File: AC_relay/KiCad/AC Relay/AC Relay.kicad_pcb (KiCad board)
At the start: 2 copper layers, 49.5 x 49.5 mm, 17 parts, among them J1 Screw_Terminal_01x02, J2 Conn_01x06_Female, J3 Screw_Terminal_01x02, K1 1461492-2, Q1 FDN537N, SW1 SW_Push, U1 BU33SD5WG-TR, U2 ESP-12E, U3 HLK-PM01

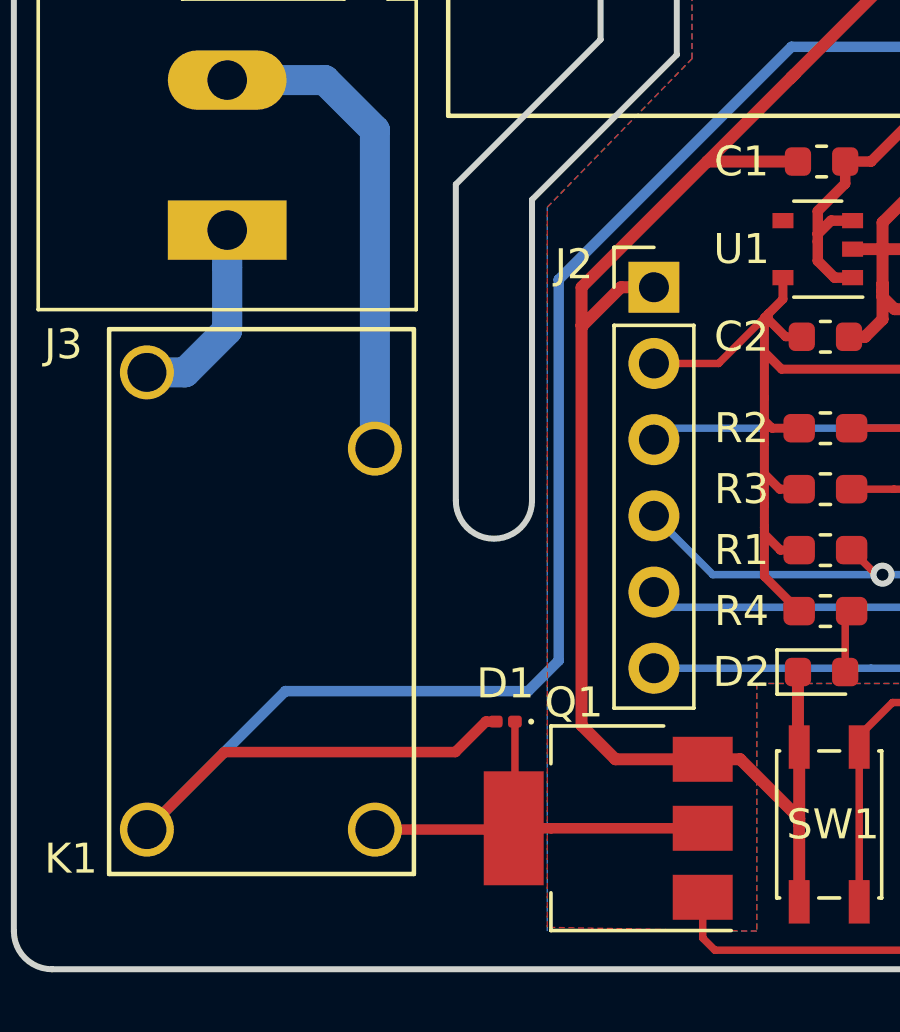
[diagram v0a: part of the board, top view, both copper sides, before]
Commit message: Diode footprint fised
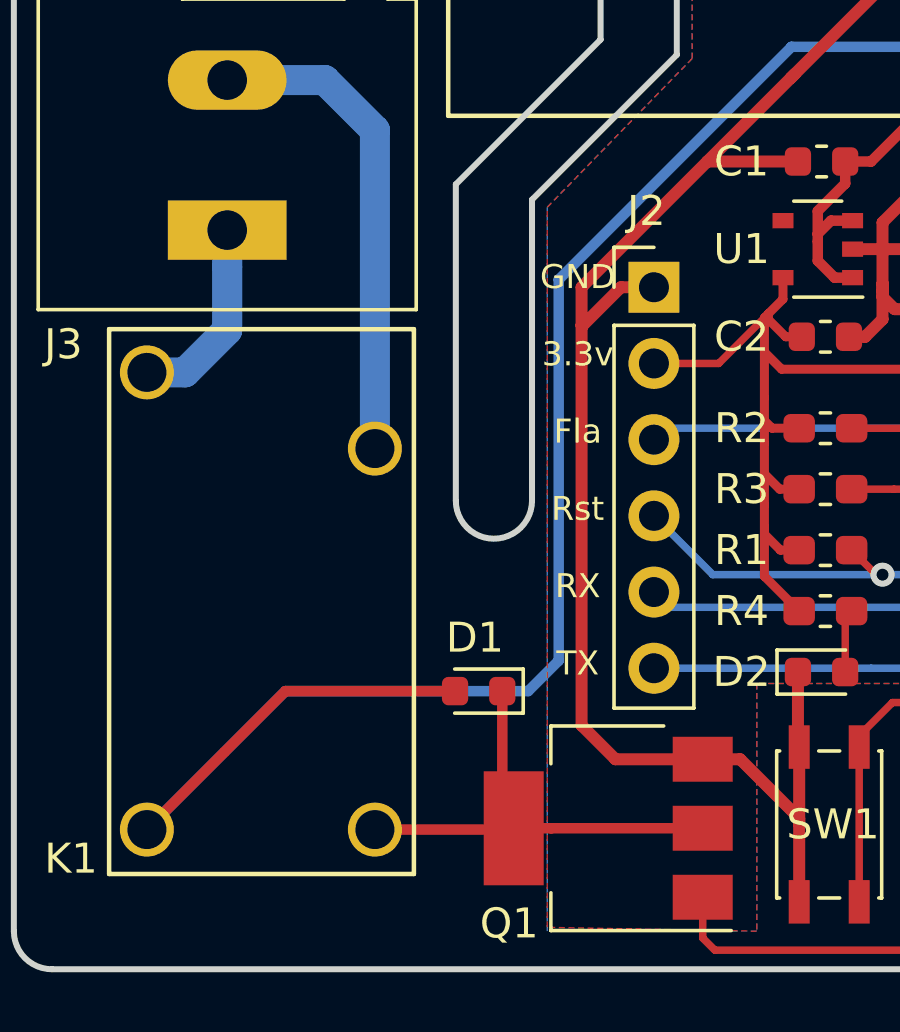
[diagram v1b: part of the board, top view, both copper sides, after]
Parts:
- D1: footprint Diode_SMD:D_0201_0603Metric -> Diode_SMD:D_0603_1608Metric
- moved D1 1.35 mm to (84.1, 87.2)
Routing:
- net Net-(D1-Pad1): track 14.5 -> 15.7 mm
- net +5V: track 99.6 -> 98.6 mm
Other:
- board text added: "AC Relay - ESP8266 Design by Enrique Gómez CC BY-SA 4.0 www.rinconingenieril.es Rev.: 2.1 - S/N:"
- board text added: "GND 3.3v Fla Rst RX TX"
- board text removed: "AC Relay - ESP8266 Design by Enrique Gómez CC BY-SA 4.0 www.rinconingenieril.es Rev.: 2.0 - S/N:"
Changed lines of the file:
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@@
   (general
     (thickness 1.6)
-    (drawings 28)
+    (drawings 29)
     (tracks 158)
     (zones 0)
@@
       (padsonsilk false)
       (subtractmaskfromsilk false)
-      (outputformat 4)
+      (outputformat 1)
       (mirror false)
       (drillshape 0)
       (scaleselection 1)
-      (outputdirectory "../../Manufacturing_GERBERs/AC_Relay/"))
+      (outputdirectory "../../Manufacturing_GERBERs/AC_Relay_V_2_1/"))
   )
   (net 0 "")
@@
     (add_net "Net-(U2-Pad9)")
   )
+  (module Diode_SMD:D_0603_1608Metric (layer F.Cu)
+    (at 84.074 87.249 180)
+    (descr "Diode SMD 0603 (1608 Metric), square (rectangular) end terminal, IPC_7351 nominal, (Body size source: http://www.tortai-tech.com/upload/download/2011102023233369053.pdf), generated with kicad-footprint-generator")
+    (tags diode)
+    (attr smd)
+    (fp_text reference D1 (at 0.127 1.778 180) (layer F.SilkS)
+      (effects (font (size 1 1) (thickness 0.15)))
+    )
+    (fp_text value RGF1B (at 0 1.43 180) (layer F.Fab)
+      (effects (font (size 1 1) (thickness 0.15)))
+    )
+    (fp_text user %R (at 0 0 180) (layer F.Fab)
+      (effects (font (size 0.4 0.4) (thickness 0.06)))
+    )
+    (fp_line (start 1.48 0.73) (end -1.48 0.73) (layer F.CrtYd) (width 0.05))
+    (fp_line (start 1.48 -0.73) (end 1.48 0.73) (layer F.CrtYd) (width 0.05))
+    (fp_line (start -1.48 -0.73) (end 1.48 -0.73) (layer F.CrtYd) (width 0.05))
+    (fp_line (start -1.48 0.73) (end -1.48 -0.73) (layer F.CrtYd) (width 0.05))
+    (fp_line (start -1.485 0.735) (end 0.8 0.735) (layer F.SilkS) (width 0.12))
+    (fp_line (start -1.485 -0.735) (end -1.485 0.735) (layer F.SilkS) (width 0.12))
+    (fp_line (start 0.8 -0.735) (end -1.485 -0.735) (layer F.SilkS) (width 0.12))
+    (fp_line (start 0.8 0.4) (end 0.8 -0.4) (layer F.Fab) (width 0.1))
+    (fp_line (start -0.8 0.4) (end 0.8 0.4) (layer F.Fab) (width 0.1))
+    (fp_line (start -0.8 -0.1) (end -0.8 0.4) (layer F.Fab) (width 0.1))
+    (fp_line (start -0.5 -0.4) (end -0.8 -0.1) (layer F.Fab) (width 0.1))
+    (fp_line (start 0.8 -0.4) (end -0.5 -0.4) (layer F.Fab) (width 0.1))
+    (pad 2 smd roundrect (at 0.7875 0 180) (size 0.875 0.95) (layers F.Cu F.Paste F.Mask) (roundrect_rratio 0.25)
+      (net 1 +5V))
+    (pad 1 smd roundrect (at -0.7875 0 180) (size 0.875 0.95) (layers F.Cu F.Paste F.Mask) (roundrect_rratio 0.25)
+      (net 2 "Net-(D1-Pad1)"))
+    (model ${KISYS3DMOD}/Diode_SMD.3dshapes/D_0603_1608Metric.wrl
+      (at (xyz 0 0 0))
+      (scale (xyz 1 1 1))
+      (rotate (xyz 0 0 0))
+    )
+  )
   (module red:HLK-PM01 (layer F.Cu)
     (at 83.058 68.072)
@@
     (descr "Through hole straight pin header, 1x06, 2.54mm pitch, single row")
     (tags "Through hole pin header THT 1x06 2.54mm single row")
-    (fp_text reference J2 (at -2.667 -0.762 180) (layer F.SilkS)
+    (fp_text reference J2 (at -0.254 -2.54 180) (layer F.SilkS)
       (effects (font (size 1 1) (thickness 0.15)))
     )
@@
       (at (xyz 0 0 0))
       (scale (xyz 1 1 1))
-      (rotate (xyz 0 0 0))
-    )
-  )
-  (module Diode_SMD:D_0201_0603Metric (layer F.Cu)
-    (at 84.963 88.265 180)
-    (descr "Diode SMD 0201 (0603 Metric), square (rectangular) end terminal, IPC_7351 nominal, (Body size source: https://www.vishay.com/docs/20052/crcw0201e3.pdf), generated with kicad-footprint-generator")
-    (tags diode)
-    (attr smd)
-    (fp_text reference D1 (at 0 1.27) (layer F.SilkS)
-      (effects (font (size 1 1) (thickness 0.15)))
-    )
-    (fp_text value RGF1B (at 0 1.05 180) (layer F.Fab) hide
-      (effects (font (size 1 1) (thickness 0.15)))
-    )
-    (fp_circle (center -0.86 0) (end -0.81 0) (layer F.SilkS) (width 0.1))
-    (fp_line (start -0.3 0.15) (end -0.3 -0.15) (layer F.Fab) (width 0.1))
-    (fp_line (start -0.3 -0.15) (end 0.3 -0.15) (layer F.Fab) (width 0.1))
-    (fp_line (start 0.3 -0.15) (end 0.3 0.15) (layer F.Fab) (width 0.1))
-    (fp_line (start 0.3 0.15) (end -0.3 0.15) (layer F.Fab) (width 0.1))
-    (fp_line (start -0.2 0.15) (end -0.2 -0.15) (layer F.Fab) (width 0.1))
-    (fp_line (start -0.1 0.15) (end -0.1 -0.15) (layer F.Fab) (width 0.1))
-    (fp_line (start -0.7 0.35) (end -0.7 -0.35) (layer F.CrtYd) (width 0.05))
-    (fp_line (start -0.7 -0.35) (end 0.7 -0.35) (layer F.CrtYd) (width 0.05))
-    (fp_line (start 0.7 -0.35) (end 0.7 0.35) (layer F.CrtYd) (width 0.05))
-    (fp_line (start 0.7 0.35) (end -0.7 0.35) (layer F.CrtYd) (width 0.05))
-    (fp_text user %R (at 0 -0.68 180) (layer F.Fab)
-      (effects (font (size 0.25 0.25) (thickness 0.04)))
-    )
-    (pad "" smd roundrect (at -0.345 0 180) (size 0.318 0.36) (layers F.Paste) (roundrect_rratio 0.25))
-    (pad "" smd roundrect (at 0.345 0 180) (size 0.318 0.36) (layers F.Paste) (roundrect_rratio 0.25))
-    (pad 1 smd roundrect (at -0.32 0 180) (size 0.46 0.4) (layers F.Cu F.Mask) (roundrect_rratio 0.25)
-      (net 2 "Net-(D1-Pad1)"))
-    (pad 2 smd roundrect (at 0.32 0 180) (size 0.46 0.4) (layers F.Cu F.Mask) (roundrect_rratio 0.25)
-      (net 1 +5V))
-    (model ${KIPRJMOD}/3dpackages/AB2_DO-214AC.wrl
-      (at (xyz 0 0 0))
-      (scale (xyz 0.1 0.1 0.1))
       (rotate (xyz 0 0 0))
     )
@@
     (tags "CMS SOT")
     (attr smd)
-    (fp_text reference Q1 (at 1.143 4.191) (layer F.SilkS)
+    (fp_text reference Q1 (at 3.302 -3.175) (layer F.SilkS)
       (effects (font (size 1 1) (thickness 0.15)))
     )
@@
     )
   )
+  (gr_text "GND\n\n3.3v\n\nFla\n\nRst\n\nRX\n\nTX" (at 87.376 79.883) (layer F.SilkS)
+    (effects (font (size 0.8 0.8) (thickness 0.125)))
+  )
   (gr_line (start 82.677 83.185) (end 82.677 69.977) (layer B.SilkS) (width 0.2))
   (gr_line (start 88.138 65.532) (end 83.312 70.358) (layer Edge.Cuts) (width 0.2))
@@
     (effects (font (size 1.5 1.5) (thickness 0.3)) (justify mirror))
   )
-  (gr_text "AC Relay - ESP8266\nDesign by Enrique Gómez\nCC BY-SA 4.0\nwww.rinconingenieril.es\nRev.: 2.0 - S/N:" (at 116.967 76.581) (layer B.SilkS)
+  (gr_text "AC Relay - ESP8266\nDesign by Enrique Gómez\nCC BY-SA 4.0\nwww.rinconingenieril.es\nRev.: 2.1 - S/N:" (at 116.967 76.581) (layer B.SilkS)
     (effects (font (size 1 1) (thickness 0.25)) (justify left mirror))
   )
@@
   (segment (start 96.2915 69.596) (end 97.155 69.596) (width 0.35) (layer F.Cu) (net 1))
   (segment (start 97.155 69.596) (end 100.979 65.772) (width 0.35) (layer F.Cu) (net 1))
-  (segment (start 84.313 88.265) (end 83.297 89.281) (width 0.35) (layer F.Cu) (net 1))
-  (segment (start 84.643 88.265) (end 84.313 88.265) (width 0.35) (layer F.Cu) (net 1))
   (segment (start 75.599 89.281) (end 73.015 91.865) (width 0.35) (layer F.Cu) (net 1))
-  (segment (start 83.297 89.281) (end 75.599 89.281) (width 0.35) (layer F.Cu) (net 1))
   (segment (start 77.631 87.249) (end 85.725 87.249) (width 0.35) (layer B.Cu) (net 1))
   (segment (start 73.015 91.865) (end 77.631 87.249) (width 0.35) (layer B.Cu) (net 1))
@@
   (segment (start 86.741 86.233) (end 86.741 73.533) (width 0.35) (layer B.Cu) (net 1))
   (segment (start 94.502 65.772) (end 114.758 65.772) (width 0.35) (layer B.Cu) (net 1))
+  (segment (start 77.631 87.249) (end 75.599 89.281) (width 0.35) (layer F.Cu) (net 1))
+  (segment (start 83.2865 87.249) (end 77.631 87.249) (width 0.35) (layer F.Cu) (net 1))
   (segment (start 86.492 91.821) (end 91.542 91.821) (width 0.35) (layer F.Cu) (net 2))
   (segment (start 85.242 91.821) (end 86.492 91.821) (width 0.35) (layer F.Cu) (net 2))
@@
   (segment (start 80.615 91.865) (end 85.198 91.865) (width 0.35) (layer F.Cu) (net 2))
   (segment (start 85.283 91.78) (end 85.242 91.821) (width 0.25) (layer F.Cu) (net 2))
-  (segment (start 85.283 88.265) (end 85.283 91.78) (width 0.25) (layer F.Cu) (net 2))
+  (segment (start 84.8615 91.4405) (end 85.242 91.821) (width 0.25) (layer F.Cu) (net 2))
+  (segment (start 84.8615 87.249) (end 84.8615 91.4405) (width 0.35) (layer F.Cu) (net 2))
   (segment (start 75.692 73.122) (end 75.692 71.882) (width 1) (layer B.Cu) (net 3))
   (segment (start 75.692 75.220792) (end 75.692 73.122) (width 1) (layer B.Cu) (net 3))
